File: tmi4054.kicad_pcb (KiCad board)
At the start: 2 copper layers, 33 x 17.2 mm, 16 parts, among them J1 USB_C_Receptacle_USB2.0, J2 Conn_01x02_Male, J3 Conn_01x02_Male, Q1 AO3401, SW1 SW_SPDT, U1 LTC4054ES5-4.2

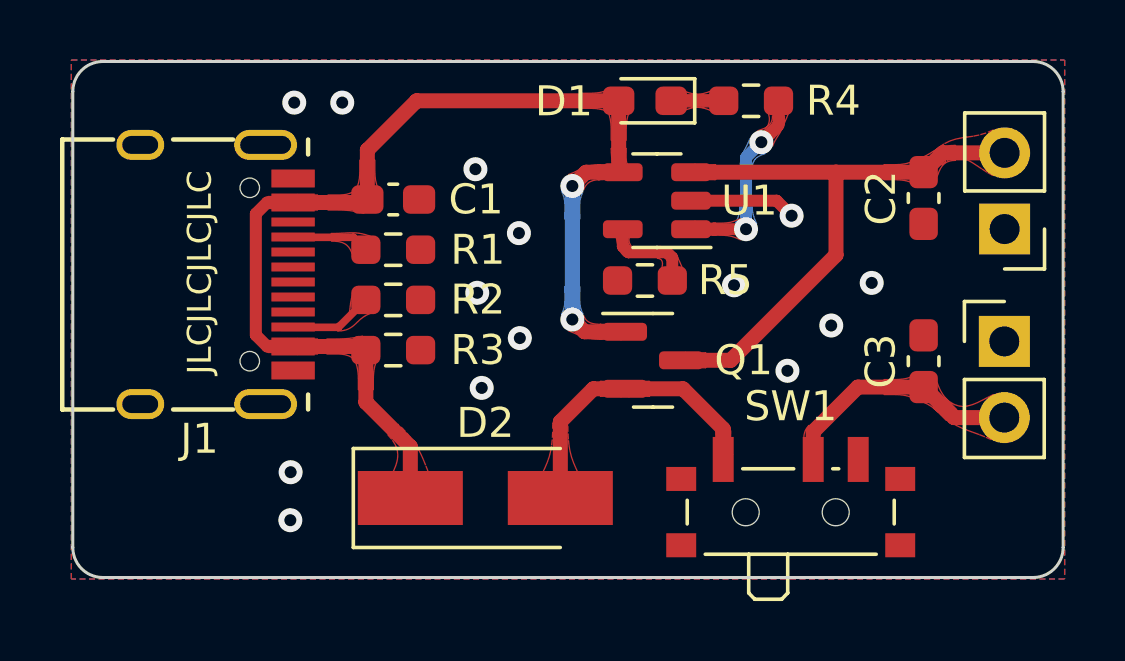
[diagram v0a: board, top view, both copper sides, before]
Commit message: adjust pmos model to AO3401A
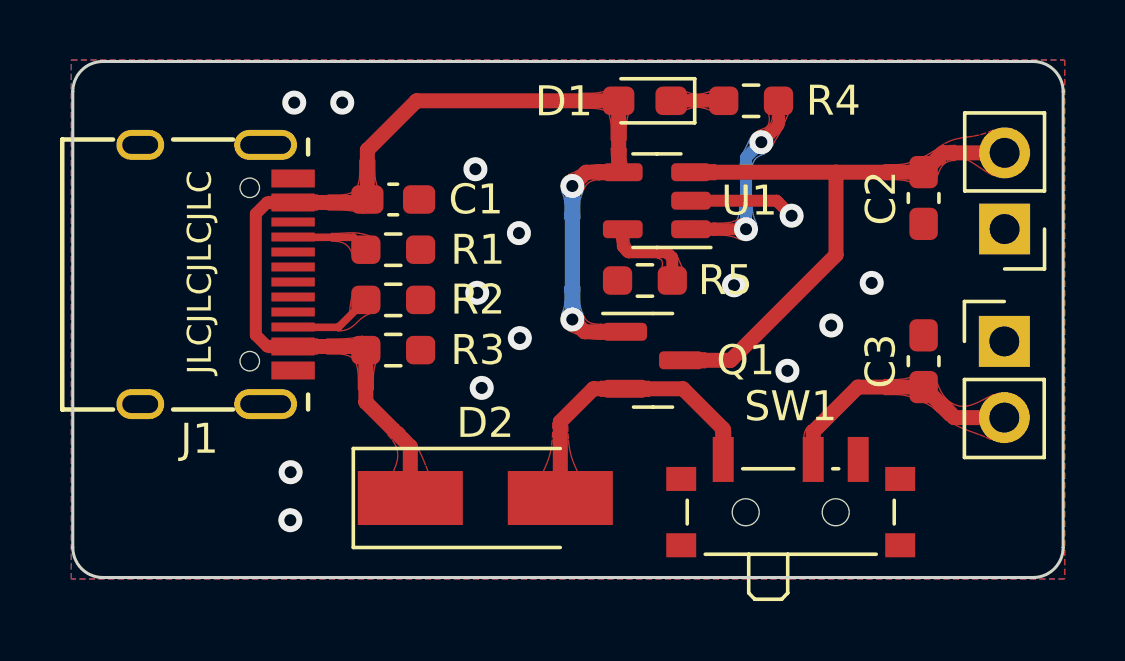
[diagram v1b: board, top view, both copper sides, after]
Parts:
- Q1: value AO3401 -> AO3401A
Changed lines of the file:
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@@
     (property "Sheetname" "")
     (attr smd)
-    (fp_text reference "Q1" (at 3.02 0) (layer "F.SilkS")
+    (fp_text reference "Q1" (at 3.09 0) (layer "F.SilkS")
       (effects (font (size 1 1) (thickness 0.15)))
     )
-    (fp_text value "AO3401" (at 0 0) (layer "F.Fab") hide
+    (fp_text value "AO3401A" (at 0 2.4) (layer "F.Fab")
       (effects (font (size 1 1) (thickness 0.15)))
     )
@@
       (effects (font (size 0.32 0.32) (thickness 0.05)))
     )
+    (fp_line (start 0 -1.56) (end -1.675 -1.56) (layer "F.SilkS") (width 0.12))
     (fp_line (start 0 1.56) (end 0.65 1.56) (layer "F.SilkS") (width 0.12))
+    (fp_line (start 0 1.56) (end -0.65 1.56) (layer "F.SilkS") (width 0.12))
     (fp_line (start 0 -1.56) (end 0.65 -1.56) (layer "F.SilkS") (width 0.12))
-    (fp_line (start 0 -1.56) (end -1.675 -1.56) (layer "F.SilkS") (width 0.12))
-    (fp_line (start 0 1.56) (end -0.65 1.56) (layer "F.SilkS") (width 0.12))
     (fp_line (start 1.92 -1.7) (end -1.92 -1.7) (layer "F.CrtYd") (width 0.05))
     (fp_line (start 1.92 1.7) (end 1.92 -1.7) (layer "F.CrtYd") (width 0.05))
     (fp_line (start -1.92 1.7) (end 1.92 1.7) (layer "F.CrtYd") (width 0.05))
     (fp_line (start -1.92 -1.7) (end -1.92 1.7) (layer "F.CrtYd") (width 0.05))
+    (fp_line (start -0.325 -1.45) (end 0.65 -1.45) (layer "F.Fab") (width 0.1))
+    (fp_line (start 0.65 1.45) (end -0.65 1.45) (layer "F.Fab") (width 0.1))
     (fp_line (start -0.65 1.45) (end -0.65 -1.125) (layer "F.Fab") (width 0.1))
-    (fp_line (start 0.65 1.45) (end -0.65 1.45) (layer "F.Fab") (width 0.1))
+    (fp_line (start 0.65 -1.45) (end 0.65 1.45) (layer "F.Fab") (width 0.1))
     (fp_line (start -0.65 -1.125) (end -0.325 -1.45) (layer "F.Fab") (width 0.1))
-    (fp_line (start -0.325 -1.45) (end 0.65 -1.45) (layer "F.Fab") (width 0.1))
-    (fp_line (start 0.65 -1.45) (end 0.65 1.45) (layer "F.Fab") (width 0.1))
     (pad "1" smd roundrect (at -0.9375 -0.95) (size 1.475 0.6) (layers "F.Cu" "F.Paste" "F.Mask") (roundrect_rratio 0.25)
       (net 4 "VCC") (pinfunction "G") (pintype "input"))
